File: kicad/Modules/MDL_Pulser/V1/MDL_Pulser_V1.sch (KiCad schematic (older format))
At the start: 21 parts, among them Q1 Q2N2222, Q2 Q2N2907, Q3 Q2N2222, Q4 Q2N2907, Q5 Q2N2222, Q6 Q2N2907, Q7 IRF9610, Q8 IRF610

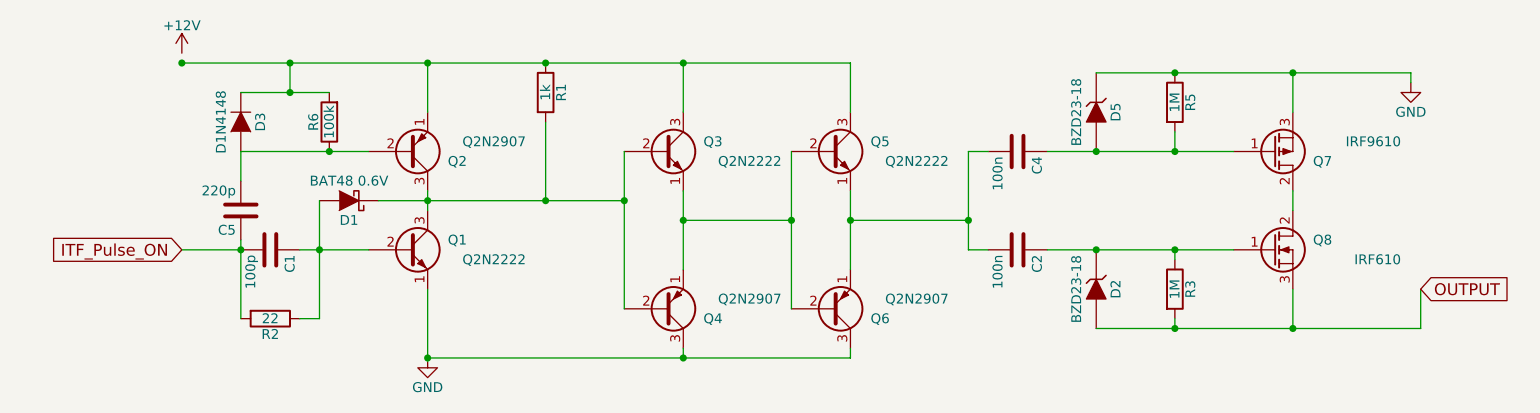
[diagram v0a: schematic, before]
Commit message: update DB_HV, update librairy and librairy path for MDL
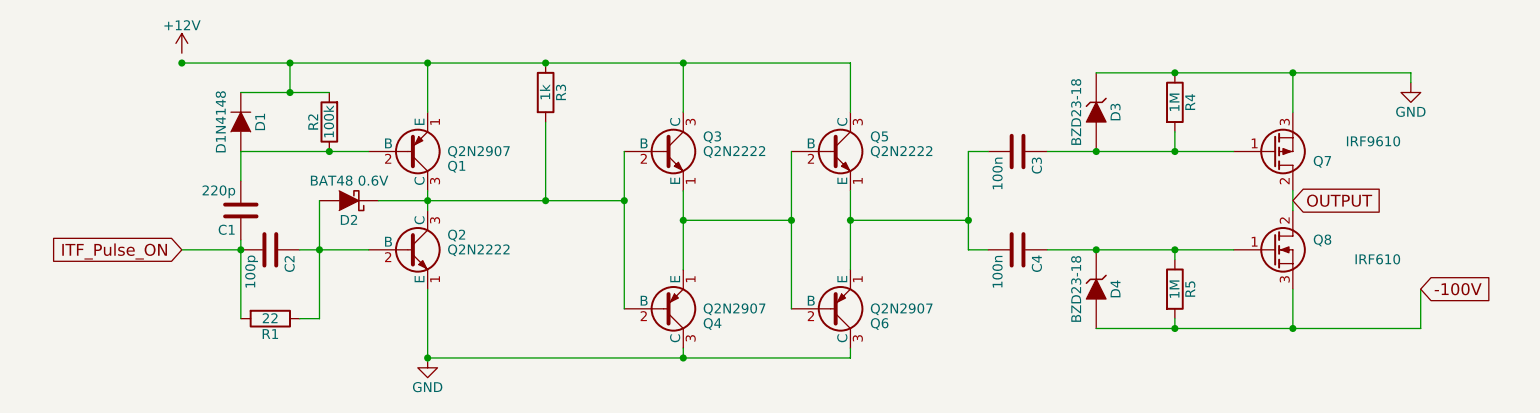
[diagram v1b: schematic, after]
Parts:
- removed Q1, Q3, Q5: Q2N2222, symbol Q_NPN_EBC
- removed Q2, Q4, Q6: Q2N2907, symbol Q_PNP_EBC
- added Q1, Q4, Q6: Q2N2907, symbol Q2N2907
- added Q2, Q3, Q5: Q2N2222, symbol Q2N2222
- renumbered C5 to C1, C1 to C2, C4 to C3, C2 to C4, D3 to D1, D1 to D2, D5 to D3, D2 to D4, R2 to R1, R6 to R2, R1 to R3, R5 to R4, R3 to R5
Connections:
- net GND: now also Q2.1 (E), Q4.3 (C), Q6.3 (C)
- net OUTPUT: now also Q7.2 (D), Q8.2 (D); no longer D4.2 (A), Q8.3 (S), R5.2
- net at C2.1, D2.2 (A), R1.1: now also Q2.2 (B)
- net at C1.2, D1.2 (A), R2.1: now also Q1.2 (B)
- net at D2.1 (K), R3.2: now also Q1.3 (C), Q2.3 (C), Q3.2 (B), Q4.2 (B)
- net at D1.1 (K), R2.2, R3.1: now also Q1.1 (E), Q3.3 (C), Q5.3 (C)
- net at C3.2, C4.2: now also Q5.1 (E), Q6.1 (E)
- new net: Q3.1 (E), Q4.1 (E), Q5.2 (B), Q6.2 (B)
- new net -100V: D4.2 (A), Q8.3 (S), R5.2
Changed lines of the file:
@@
 LIBS:contrib
 LIBS:valves
+LIBS:echopen
+LIBS:MDL_Pulser_V1-cache
 EELAYER 25 0
 EELAYER END
@@
 $EndDescr
 $Comp
-L R R2
+L R R1
 U 1 1 5762AE47
 P 1650 3200
-F 0 "R2" V 1730 3200 50  0000 C CNN
+F 0 "R1" V 1730 3200 50  0000 C CNN
 F 1 "22" V 1650 3200 50  0000 C CNN
 F 2 "" V 1580 3200 50  0000 C CNN
@@
 $EndComp
 $Comp
-L C C1
+L C C2
 U 1 1 5762AFD3
 P 1650 2850
-F 0 "C1" H 1675 2950 50  0000 L CNN
+F 0 "C2" H 1675 2950 50  0000 L CNN
 F 1 "100p" H 1675 2750 50  0000 L CNN
 F 2 "" H 1688 2700 50  0000 C CNN
@@
 $EndComp
 $Comp
-L C C5
+L C C1
 U 1 1 5762B0B6
 P 1500 2650
-F 0 "C5" H 1525 2750 50  0000 L CNN
+F 0 "C1" H 1525 2750 50  0000 L CNN
 F 1 "220p" H 1525 2550 50  0000 L CNN
 F 2 "" H 1538 2500 50  0000 C CNN
@@
 $EndComp
 $Comp
-L D_Schottky D1
+L D_Schottky D2
 U 1 1 5762B16F
 P 2050 2600
-F 0 "D1" H 2050 2700 50  0000 C CNN
+F 0 "D2" H 2050 2700 50  0000 C CNN
 F 1 "BAT48 0.6V" H 2050 2500 50  0000 C CNN
 F 2 "" H 2050 2600 50  0000 C CNN
@@
 $EndComp
 $Comp
-L D D3
+L D D1
 U 1 1 5762B35A
 P 1500 2200
-F 0 "D3" H 1500 2300 50  0000 C CNN
+F 0 "D1" H 1500 2300 50  0000 C CNN
 F 1 "D1N4148" H 1500 2100 50  0000 C CNN
 F 2 "" H 1500 2200 50  0000 C CNN
@@
 $EndComp
 $Comp
-L R R6
+L R R2
 U 1 1 5762B412
 P 1950 2200
-F 0 "R6" V 2030 2200 50  0000 C CNN
+F 0 "R2" V 2030 2200 50  0000 C CNN
 F 1 "100k" V 1950 2200 50  0000 C CNN
 F 2 "" V 1880 2200 50  0000 C CNN
@@
 $EndComp
 $Comp
-L R R1
+L R R3
 U 1 1 5762B4D5
 P 3050 2050
-F 0 "R1" V 3130 2050 50  0000 C CNN
+F 0 "R3" V 3130 2050 50  0000 C CNN
 F 1 "1k" V 3050 2050 50  0000 C CNN
 F 2 "" V 2980 2050 50  0000 C CNN
@@
 	1    0    0    -1
 $EndComp
-$Comp
-L Q_NPN_EBC Q1
-U 1 1 5762B56E
-P 2350 2850
-F 0 "Q1" H 2650 2900 50  0000 R CNN
-F 1 "Q2N2222" H 2950 2800 50  0000 R CNN
-F 2 "" H 2550 2950 50  0000 C CNN
-F 3 "" H 2350 2850 50  0000 C CNN
-	1    2350 2850
-	1    0    0    -1
-$EndComp
-$Comp
-L Q_PNP_EBC Q2
-U 1 1 5762B5CF
-P 2350 2350
-F 0 "Q2" H 2650 2400 50  0000 R CNN
-F 1 "Q2N2907" H 2950 2300 50  0000 R CNN
-F 2 "" H 2550 2450 50  0000 C CNN
-F 3 "" H 2350 2350 50  0000 C CNN
-	1    2350 2350
-	1    0    0    1
-$EndComp
 Wire Wire Line
 	2450 2550 2450 2650
@@
 Connection ~ 1950 2350
 Wire Wire Line
-	2450 2150 2450 1900
+	2450 1900 2450 2150
 Wire Wire Line
 	1200 1900 4600 1900
@@
 Wire Wire Line
 	1500 2850 1200 2850
-$Comp
-L Q_PNP_EBC Q4
-U 1 1 5762BC88
-P 3650 3150
-F 0 "Q4" H 3950 3200 50  0000 R CNN
-F 1 "Q2N2907" H 4250 3100 50  0000 R CNN
-F 2 "" H 3850 3250 50  0000 C CNN
-F 3 "" H 3650 3150 50  0000 C CNN
-	1    3650 3150
-	1    0    0    1
-$EndComp
-$Comp
-L Q_PNP_EBC Q6
-U 1 1 5762BD05
-P 4500 3150
-F 0 "Q6" H 4800 3200 50  0000 R CNN
-F 1 "Q2N2907" H 5100 3100 50  0000 R CNN
-F 2 "" H 4700 3250 50  0000 C CNN
-F 3 "" H 4500 3150 50  0000 C CNN
-	1    4500 3150
-	1    0    0    1
-$EndComp
-$Comp
-L Q_NPN_EBC Q3
-U 1 1 5762BD85
-P 3650 2350
-F 0 "Q3" H 3950 2400 50  0000 R CNN
-F 1 "Q2N2222" H 4250 2300 50  0000 R CNN
-F 2 "" H 3850 2450 50  0000 C CNN
-F 3 "" H 3650 2350 50  0000 C CNN
-	1    3650 2350
-	1    0    0    -1
-$EndComp
-$Comp
-L Q_NPN_EBC Q5
-U 1 1 5762BDF6
-P 4500 2350
-F 0 "Q5" H 4800 2400 50  0000 R CNN
-F 1 "Q2N2222" H 5100 2300 50  0000 R CNN
-F 2 "" H 4700 2450 50  0000 C CNN
-F 3 "" H 4500 2350 50  0000 C CNN
-	1    4500 2350
-	1    0    0    -1
-$EndComp
 Wire Wire Line
 	3750 1900 3750 2150
@@
 Connection ~ 3050 2600
 $Comp
-L C C2
+L C C4
 U 1 1 5767D1D8
 P 5450 2850
-F 0 "C2" H 5475 2950 50  0000 L CNN
+F 0 "C4" H 5475 2950 50  0000 L CNN
 F 1 "100n" H 5475 2750 50  0000 L CNN
 F 2 "" H 5488 2700 50  0000 C CNN
@@
 $EndComp
 $Comp
-L C C4
+L C C3
 U 1 1 5767D253
 P 5450 2350
-F 0 "C4" H 5475 2450 50  0000 L CNN
+F 0 "C3" H 5475 2450 50  0000 L CNN
 F 1 "100n" H 5475 2250 50  0000 L CNN
 F 2 "" H 5488 2200 50  0000 C CNN
@@
 Connection ~ 5200 2700
 $Comp
-L ZENER D5
+L ZENER D3
 U 1 1 5767D3BA
 P 5850 2150
-F 0 "D5" H 5850 2250 50  0000 C CNN
+F 0 "D3" H 5850 2250 50  0000 C CNN
 F 1 "BZD23-18" H 5850 2050 50  0000 C CNN
 F 2 "" H 5850 2150 50  0000 C CNN
@@
 $EndComp
 $Comp
-L ZENER D2
+L ZENER D4
 U 1 1 5767D8BC
 P 5850 3050
-F 0 "D2" H 5850 3150 50  0000 C CNN
+F 0 "D4" H 5850 3150 50  0000 C CNN
 F 1 "BZD23-18" H 5850 2950 50  0000 C CNN
 F 2 "" H 5850 3050 50  0000 C CNN
@@
 	5600 2850 6550 2850
 $Comp
-L R R5
+L R R4
 U 1 1 5767E1A7
 P 6250 2100
-F 0 "R5" V 6330 2100 50  0000 C CNN
+F 0 "R4" V 6330 2100 50  0000 C CNN
 F 1 "1M" V 6250 2100 50  0000 C CNN
 F 2 "" V 6180 2100 50  0000 C CNN
@@
 $EndComp
 $Comp
-L R R3
+L R R5
 U 1 1 5767E21C
 P 6250 3050
-F 0 "R3" V 6330 3050 50  0000 C CNN
+F 0 "R5" V 6330 3050 50  0000 C CNN
 F 1 "1M" V 6250 3050 50  0000 C CNN
 F 2 "" V 6180 3050 50  0000 C CNN
@@
 	2450 3400 4600 3400
 Text GLabel 7500 3050 2    60   Input ~ 0
+-100V
+$Comp
+L Q2N2907 Q1
+U 1 1 57B4374C
+P 2350 2350
+F 0 "Q1" H 2550 2425 50  0000 L CNN
+F 1 "Q2N2907" H 2550 2350 50  0000 L CNN
+F 2 "" H 2650 2200 50  0000 L CIN
+F 3 "" H 2350 2350 50  0000 L CNN
+	1    2350 2350
+	1    0    0    1
+$EndComp
+$Comp
+L Q2N2222 Q2
+U 1 1 57B438E6
+P 2350 2850
+F 0 "Q2" H 2550 2925 50  0000 L CNN
+F 1 "Q2N2222" H 2550 2850 50  0000 L CNN
+F 2 "" H 2550 2775 50  0000 L CIN
+F 3 "" H 2350 2850 50  0000 L CNN
+	1    2350 2850
+	1    0    0    -1
+$EndComp
+$Comp
+L Q2N2222 Q3
+U 1 1 57B43952
+P 3650 2350
+F 0 "Q3" H 3850 2425 50  0000 L CNN
+F 1 "Q2N2222" H 3850 2350 50  0000 L CNN
+F 2 "" H 3850 2275 50  0000 L CIN
+F 3 "" H 3650 2350 50  0000 L CNN
+	1    3650 2350
+	1    0    0    -1
+$EndComp
+$Comp
+L Q2N2222 Q5
+U 1 1 57B439F8
+P 4500 2350
+F 0 "Q5" H 4700 2425 50  0000 L CNN
+F 1 "Q2N2222" H 4700 2350 50  0000 L CNN
+F 2 "" H 4700 2275 50  0000 L CIN
+F 3 "" H 4500 2350 50  0000 L CNN
+	1    4500 2350
+	1    0    0    -1
+$EndComp
+$Comp
+L Q2N2907 Q4
+U 1 1 57B43ABF
+P 3650 3150
+F 0 "Q4" H 3850 3225 50  0000 L CNN
+F 1 "Q2N2907" H 3850 3150 50  0000 L CNN
+F 2 "" H 3950 3000 50  0000 L CIN
+F 3 "" H 3650 3150 50  0000 L CNN
+	1    3650 3150
+	1    0    0    1
+$EndComp
+$Comp
+L Q2N2907 Q6
+U 1 1 57B43B90
+P 4500 3150
+F 0 "Q6" H 4700 3225 50  0000 L CNN
+F 1 "Q2N2907" H 4700 3150 50  0000 L CNN
+F 2 "" H 4800 3000 50  0000 L CIN
+F 3 "" H 4500 3150 50  0000 L CNN
+	1    4500 3150
+	1    0    0    1
+$EndComp
+Text GLabel 6850 2600 2    60   Input ~ 0
 OUTPUT
 $EndSCHEMATC

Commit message: update MDLs with new librairy
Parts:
- removed Q1, Q4, Q6: Q2N2907, symbol Q2N2907
- removed Q2, Q3, Q5: Q2N2222, symbol Q2N2222
- added Q1, Q4, Q6: 2N2907, symbol 2N2907
- added Q2, Q3, Q5: 2N2222, symbol 2N2222
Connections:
- net GND: now also Q2.1 (E), Q4.3 (C), Q6.3 (C)
- net at C2.1, D2.2 (A), R1.1: now also Q2.2 (B)
- net at C1.2, D1.2 (A), R2.1: now also Q1.2 (B)
- net at D2.1 (K), R3.2: now also Q1.3 (C), Q2.3 (C), Q3.2 (B), Q4.2 (B)
- net at D1.1 (K), R2.2, R3.1: now also Q1.1 (E), Q3.3 (C), Q5.3 (C)
- net at C3.2, C4.2: now also Q5.1 (E), Q6.1 (E)
- new net: Q3.1 (E), Q4.1 (E), Q5.2 (B), Q6.2 (B)
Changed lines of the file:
@@
 Text GLabel 7500 3050 2    60   Input ~ 0
 -100V
+Text GLabel 6850 2600 2    60   Input ~ 0
+OUTPUT
 $Comp
-L Q2N2907 Q1
-U 1 1 57B4374C
+L 2N2907 Q1
+U 1 1 57B47406
 P 2350 2350
 F 0 "Q1" H 2550 2425 50  0000 L CNN
-F 1 "Q2N2907" H 2550 2350 50  0000 L CNN
+F 1 "2N2907" H 2550 2350 50  0000 L CNN
 F 2 "" H 2650 2200 50  0000 L CIN
 F 3 "" H 2350 2350 50  0000 L CNN
@@
 $EndComp
 $Comp
-L Q2N2222 Q2
-U 1 1 57B438E6
+L 2N2222 Q2
+U 1 1 57B474B8
 P 2350 2850
 F 0 "Q2" H 2550 2925 50  0000 L CNN
-F 1 "Q2N2222" H 2550 2850 50  0000 L CNN
+F 1 "2N2222" H 2550 2850 50  0000 L CNN
 F 2 "" H 2550 2775 50  0000 L CIN
 F 3 "" H 2350 2850 50  0000 L CNN
@@
 $EndComp
 $Comp
-L Q2N2222 Q3
-U 1 1 57B43952
+L 2N2222 Q3
+U 1 1 57B47ACD
 P 3650 2350
 F 0 "Q3" H 3850 2425 50  0000 L CNN
-F 1 "Q2N2222" H 3850 2350 50  0000 L CNN
+F 1 "2N2222" H 3850 2350 50  0000 L CNN
 F 2 "" H 3850 2275 50  0000 L CIN
 F 3 "" H 3650 2350 50  0000 L CNN
@@
 $EndComp
 $Comp
-L Q2N2222 Q5
-U 1 1 57B439F8
+L 2N2222 Q5
+U 1 1 57B47B41
 P 4500 2350
 F 0 "Q5" H 4700 2425 50  0000 L CNN
-F 1 "Q2N2222" H 4700 2350 50  0000 L CNN
+F 1 "2N2222" H 4700 2350 50  0000 L CNN
 F 2 "" H 4700 2275 50  0000 L CIN
 F 3 "" H 4500 2350 50  0000 L CNN
@@
 $EndComp
 $Comp
-L Q2N2907 Q4
-U 1 1 57B43ABF
+L 2N2907 Q4
+U 1 1 57B47BAB
 P 3650 3150
 F 0 "Q4" H 3850 3225 50  0000 L CNN
-F 1 "Q2N2907" H 3850 3150 50  0000 L CNN
+F 1 "2N2907" H 3850 3150 50  0000 L CNN
 F 2 "" H 3950 3000 50  0000 L CIN
 F 3 "" H 3650 3150 50  0000 L CNN
@@
 $EndComp
 $Comp
-L Q2N2907 Q6
-U 1 1 57B43B90
+L 2N2907 Q6
+U 1 1 57B47C78
 P 4500 3150
 F 0 "Q6" H 4700 3225 50  0000 L CNN
-F 1 "Q2N2907" H 4700 3150 50  0000 L CNN
+F 1 "2N2907" H 4700 3150 50  0000 L CNN
 F 2 "" H 4800 3000 50  0000 L CIN
 F 3 "" H 4500 3150 50  0000 L CNN
@@
 	1    0    0    1
 $EndComp
-Text GLabel 6850 2600 2    60   Input ~ 0
-OUTPUT
 $EndSCHEMATC
